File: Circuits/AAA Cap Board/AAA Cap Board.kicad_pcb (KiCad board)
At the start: 2 copper layers, 86.9 x 20.8 mm, 0 parts

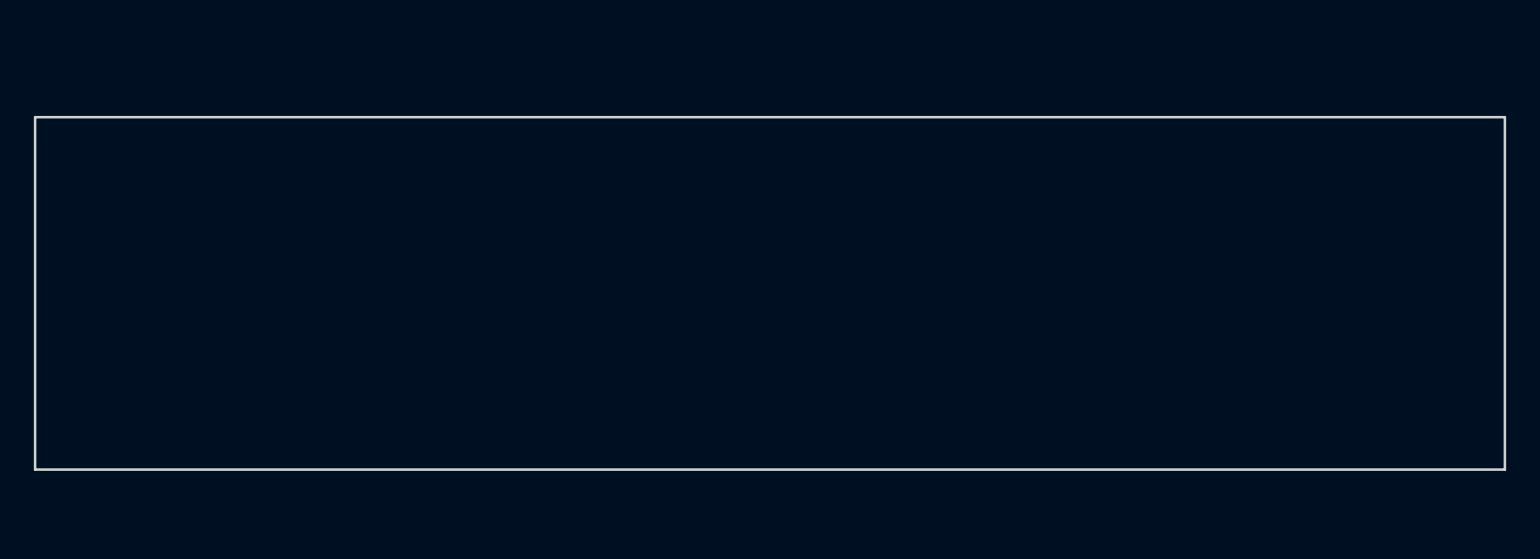
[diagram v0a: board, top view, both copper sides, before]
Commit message: Circuits: Updating AAA Cap Board PCB
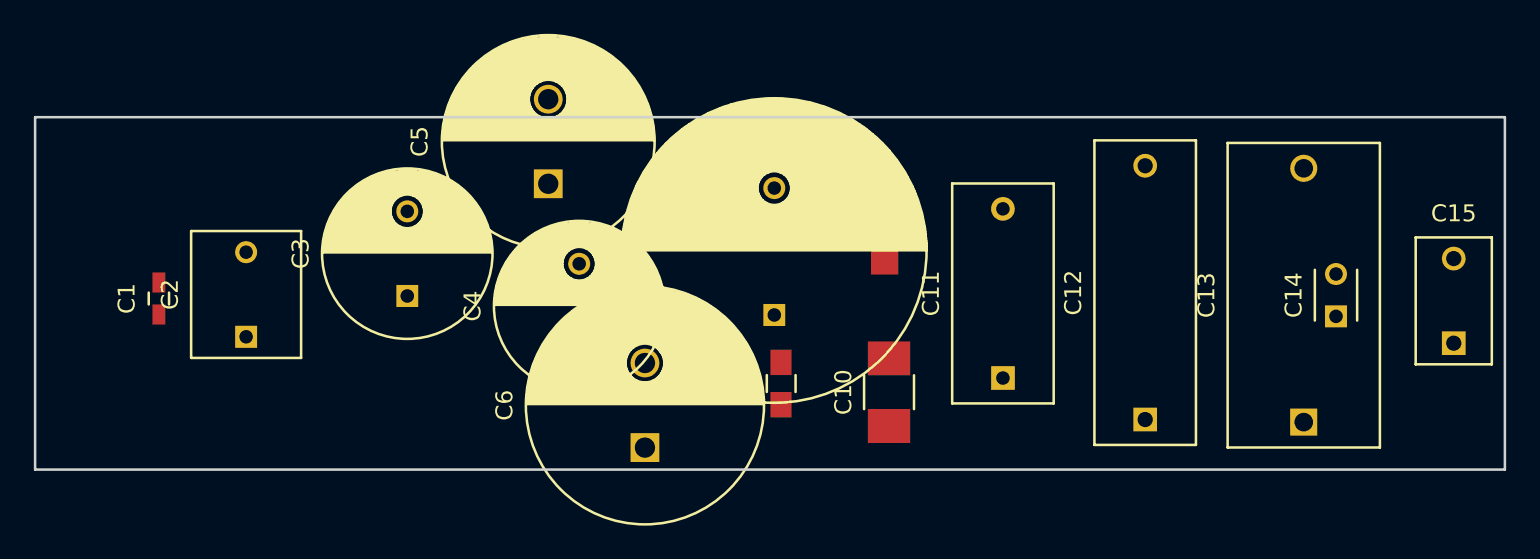
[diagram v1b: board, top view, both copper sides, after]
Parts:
- added C1: C, Capacitors_SMD:C_0603_HandSoldering, F.Cu at (133.8, 97.1)
- added C10: C, Capacitors_SMD:C_1210_HandSoldering, F.Cu at (177.0, 102.6)
- added C11: CP, Capacitors_ThroughHole:C_Rect_L13_W6_H12_P10, F.Cu at (183.7, 101.8)
- added C12: CP, Capacitors_ThroughHole:C_Rect_L18_W6_H12_P15, F.Cu at (192.1, 104.2)
- added C13: CP, Capacitors_ThroughHole:C_Rect_L18_W9_H15_P15, F.Cu at (201.5, 104.4)
- added C14: C, Capacitors_ThroughHole:C_Disc_D3_P2.5, F.Cu at (203.4, 98.1)
- added C15: C, Capacitors_ThroughHole:C_Disc_D7.5_P5, F.Cu at (210.3, 99.7)
- added C2: CP, Capacitors_ThroughHole:C_Rect_L7.5_W6.5_P5, F.Cu at (139.0, 99.3)
- added C3: CP1, Capacitors_ThroughHole:C_Radial_D10_L13_P5, F.Cu at (148.5, 96.9)
- added C4: CP1, Capacitors_ThroughHole:C_Radial_D10_L16_P5, F.Cu at (158.6, 100.0)
- added C5: CP1, Capacitors_ThroughHole:C_Radial_D12.5_L25_P5, F.Cu at (156.8, 90.3)
- added C6: CP1, Capacitors_ThroughHole:C_Radial_D14_L25_P5, F.Cu at (162.5, 105.9)
- added C7: CP1, Capacitors_ThroughHole:C_Radial_D18_L36_P7.5, F.Cu at (170.2, 98.1)
- added C8: C, Capacitors_SMD:C_0805_HandSoldering, F.Cu at (170.6, 102.1)
- added C9: C, Capacitors_SMD:C_1206_HandSoldering, F.Cu at (176.7, 92.7)
